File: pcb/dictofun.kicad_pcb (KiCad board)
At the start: 4 copper layers, 40 x 20 mm, 132 parts, among them J1 Conn_01x01_Female, J3 USB_B_Micro, J4 Conn_01x02_Socket, J5 Conn_01x03_Socket, Q1 PMOS, U2 W25Q128JWPIQ, U3 TPS63802DLAR, U4 BQ24078RGTR, U5 RV-4162-C7, U6 SN74LVC1G79DBVT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

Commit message: Design Freeze DF 1.4
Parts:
- S1: footprint _other:SW_KMR221GLFS -> df_components:SW_KMR221GLFS
- U3: footprint _other:VREG_TPS63802DLAR -> df_components:VREG_TPS63802DLAR
- moved RN3 0.12 mm to (125.0, 96.5)
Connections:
- U5 pad 2: /RTC_CLKOUT -> unconnected-(U5-CLKOUT-Pad2)
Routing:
- net Net-(D4-BK): track 3.55 -> 4.55 mm
- net /Power/FF_Q: track 4.91 -> 5.69 mm
- net /PDM_CLK: track 12.6 -> 13.3 mm
- net Net-(D4-GK): track 3.81 -> 4.35 mm

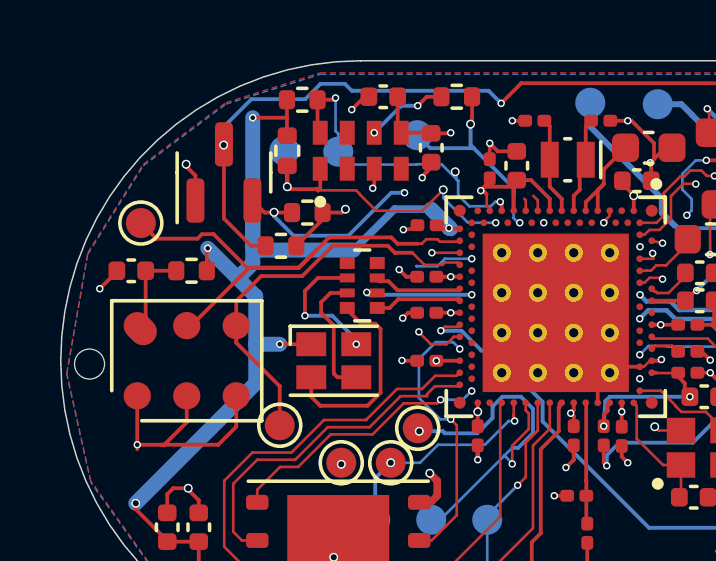
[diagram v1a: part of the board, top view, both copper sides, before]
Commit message: fixed error: RTC PFET could shorten battery to the ground
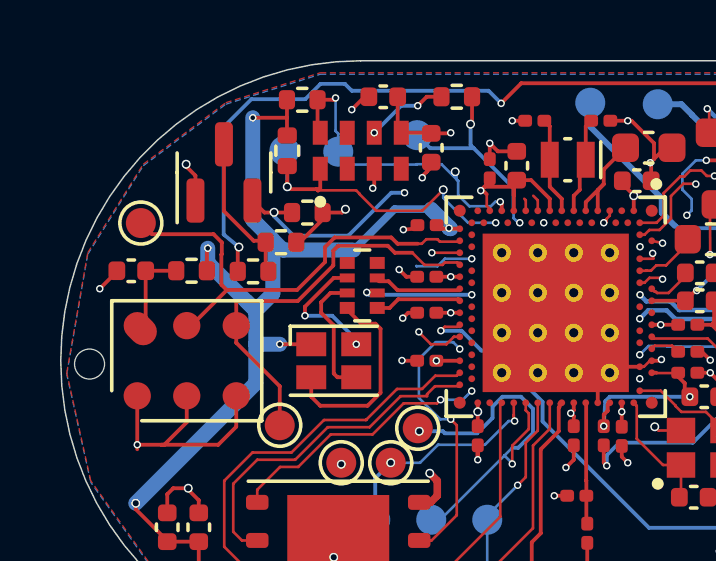
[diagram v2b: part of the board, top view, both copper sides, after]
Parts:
- added R25: 330, Resistor_SMD:R_0402_1005Metric, F.Cu at (121.4, 96.0)
- moved R24 0.12 mm to (122.3, 95.0)
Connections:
- Q1 pad 3: VREG_EN -> Net-(Q1-S)
- R24 pad 2: VREG_EN -> Net-(Q1-S)
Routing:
- net Net-(Q1-S): track 0.00 -> 5.10 mm
- net /PDM_DATA: track 17.4 -> 15.4 mm
- net VCC: track 132.3 -> 133.2 mm

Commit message: fixed another issue (added current limiting resistor, added testpoint for button control)
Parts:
- added TP33: TestPoint, TestPoint:TestPoint_Pad_D1.0mm, B.Cu at (143.8, 99.0)
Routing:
- net /BUTTON_INPUT: vias 2 -> 3
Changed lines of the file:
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@@
     (pad_to_mask_clearance 0)
     (pcbplotparams
-      (layerselection 0x00010fc_ffffffff)
+      (layerselection 0x0001000_fffffff8)
       (plot_on_all_layers_selection 0x0000000_00000000)
       (disableapertmacros false)
@@
       (sketchpadsonfab false)
       (subtractmaskfromsilk false)
-      (outputformat 1)
+      (outputformat 3)
       (mirror false)
       (drillshape 0)
       (scaleselection 1)
-      (outputdirectory "out/v1.4/gerber")
+      (outputdirectory "out/v1.4_fixture/")
     )
   )
@@
     (descr "LED SMD 0603 (1608 Metric), square (rectangular) end terminal, IPC_7351 nominal, (Body size source: http://www.tortai-tech.com/upload/download/2011102023233369053.pdf), generated with kicad-footprint-generator")
     (tags "LED")
-    (property "LCSC" "C72043")
+    (property "LCSC" "C131282")
+    (property "Populate" "")
     (property "Sheetfile" "power.kicad_sch")
     (property "Sheetname" "Power")
@@
     (descr "Capacitor SMD 0201 (0603 Metric), square (rectangular) end terminal, IPC_7351 nominal, (Body size source: https://www.vishay.com/docs/20052/crcw0201e3.pdf), generated with kicad-footprint-generator")
     (tags "capacitor")
-    (property "LCSC" "")
+    (property "LCSC" "C161369")
     (property "Populate" "")
     (property "Sheetfile" "dictofun.kicad_sch")
@@
     (descr "Capacitor SMD 0201 (0603 Metric), square (rectangular) end terminal, IPC_7351 nominal, (Body size source: https://www.vishay.com/docs/20052/crcw0201e3.pdf), generated with kicad-footprint-generator")
     (tags "capacitor")
-    (property "LCSC" "")
+    (property "LCSC" "C384700")
     (property "Populate" "")
     (property "Sheetfile" "dictofun.kicad_sch")
@@
     (descr "Inductor SMD 0201 (0603 Metric), square (rectangular) end terminal, IPC_7351 nominal, (Body size source: https://www.vishay.com/docs/20052/crcw0201e3.pdf), generated with kicad-footprint-generator")
     (tags "inductor")
-    (property "LCSC" "")
+    (property "LCSC" "C1329438")
     (property "Populate" "")
     (property "Sheetfile" "dictofun.kicad_sch")
@@
     (property "Check_prices" "https://www.snapeda.com/parts/NRF5340-QKAA-R7/Nordic+Semiconductor+ASA/view-part/?ref=eda")
     (property "Description" "\nRF System on a Chip - SoC Dual-core Bluetooth 5.2 SoC supporting Bluetooth Low Energy, Bluetooth mesh, NFC, Thread, and Zigbee\n")
+    (property "LCSC" "C3015611")
     (property "MANUFACTURER" "Nordic Semiconductor")
     (property "MAXIMUM_PACKAGE_HEIGHT" "0.85mm")
@@
   )
   (footprint "TestPoint:TestPoint_Pad_D1.0mm" (layer "B.Cu")
+    (at 143.77 99 180)
+    (descr "SMD pad as test Point, diameter 1.0mm")
+    (tags "test point SMD pad")
+    (property "Sheetfile" "dictofun.kicad_sch")
+    (property "Sheetname" "")
+    (property "ki_description" "test point")
+    (property "ki_keywords" "test point tp")
+    (attr exclude_from_pos_files)
+    (fp_text reference "TP33" (at 0 1.448) (layer "B.SilkS") hide
+        (effects (font (size 1 1) (thickness 0.15)) (justify mirror))
+    )
+    (fp_text value "TestPoint" (at 0 -1.55) (layer "B.Fab")
+        (effects (font (size 1 1) (thickness 0.15)) (justify mirror))
+    )
+    (fp_text user "${REFERENCE}" (at 0 1.45) (layer "B.Fab")
+        (effects (font (size 1 1) (thickness 0.15)) (justify mirror))
+    )
+    (fp_circle (center 0 0) (end 0 -0.7)
+      (stroke (width 0.12) (type solid)) (fill none) (layer "B.SilkS"))
+    (fp_circle (center 0 0) (end 1 0)
+      (stroke (width 0.05) (type solid)) (fill none) (layer "B.CrtYd"))
+    (pad "1" smd circle (at 0 0 180) (size 1 1) (layers "B.Cu" "B.Mask")
+      (net 49 "/BUTTON_INPUT") (pinfunction "1") (pintype "passive"))
+  )
+  (footprint "TestPoint:TestPoint_Pad_D1.0mm" (layer "B.Cu")
     (at 142 104.9 180)
     (descr "SMD pad as test Point, diameter 1.0mm")
@@
   (segment (start 122.878262 96.64) (end 120.53 96.64) (width 0.127) (layer "F.Cu") (net 48))
   (segment (start 141.55 102.22) (end 140.98 102.79) (width 0.254) (layer "F.Cu") (net 49))
+  (segment (start 143.825 98.935) (end 143.77 98.99) (width 0.254) (layer "F.Cu") (net 49))
   (segment (start 140.98 102.79) (end 140.98 103.77) (width 0.254) (layer "F.Cu") (net 49))
+  (segment (start 143.825 99.045) (end 143.825 101.05) (width 0.254) (layer "F.Cu") (net 49))
   (segment (start 153.4 99.8) (end 153.41 99.79) (width 0.127) (layer "F.Cu") (net 49))
   (segment (start 154.1 98.48) (end 154.1 99.79) (width 0.127) (layer "F.Cu") (net 49))
@@
   (segment (start 153.3 99.8) (end 153.4 99.8) (width 0.127) (layer "F.Cu") (net 49))
   (segment (start 143.825 101.275) (end 142.88 102.22) (width 0.254) (layer "F.Cu") (net 49))
-  (segment (start 143.825 96.95) (end 143.825 101.05) (width 0.254) (layer "F.Cu") (net 49))
+  (segment (start 143.77 98.99) (end 143.825 99.045) (width 0.254) (layer "F.Cu") (net 49))
+  (segment (start 143.825 96.95) (end 143.825 98.935) (width 0.254) (layer "F.Cu") (net 49))
   (segment (start 142.88 102.22) (end 141.55 102.22) (width 0.254) (layer "F.Cu") (net 49))
   (via (at 152.15 100.94) (size 0.25) (drill 0.15) (layers "F.Cu" "B.Cu") (net 49))
+  (via (at 143.77 98.99) (size 0.3) (drill 0.2) (layers "F.Cu" "B.Cu") (net 49))
   (via (at 143.84023 101.085418) (size 0.25) (drill 0.15) (layers "F.Cu" "B.Cu") (net 49))
   (segment (start 144.7685 101.6485) (end 144.75 101.63) (width 0.127) (layer "In1.Cu") (net 49))

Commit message: df 1.4.52840 ready for production
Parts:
- removed C30, C31, C32, C33, C34, C35, C45: 100n, Capacitor_SMD:C_0201_0603Metric
- removed C36: N.C, Capacitor_SMD:C_0201_0603Metric
- removed C37, C38, C39, C40, C44: 1u, Capacitor_SMD:C_0402_1005Metric
- removed C39(NP0)1: 100pF, Capacitor_SMD:C_0201_0603Metric
- removed C41: 2.2u, Capacitor_SMD:C_0603_1608Metric
- removed C42, C43: 4.7u, Capacitor_SMD:C_0603_1608Metric
- removed L4: 10uH, Inductor_SMD:L_0603_1608Metric
- removed L5, L6: 15nH, Inductor_SMD:L_0201_0603Metric
- removed R20: 4.7, Resistor_SMD:R_0201_0603Metric
- removed TP11, TP20, TP30, TP31: TestPoint, TestPoint:TestPoint_Pad_D1.0mm
- removed U7: NRF5340-QKAA-R7, _other:XCVR_NRF5340-QKAA-R7
- added C14: 1uF, Capacitor_SMD:C_0402_1005Metric, F.Cu at (138.8, 94.3)
- added C16: N.C, Capacitor_SMD:C_0402_1005Metric, F.Cu at (137.6, 98.7)
- added C22: 100nF, Capacitor_SMD:C_0402_1005Metric, F.Cu at (137.6, 99.7)
- added C48: N.C, Capacitor_SMD:C_0402_1005Metric, F.Cu at (134.2, 102.2)
- added C49: 820pF, Capacitor_SMD:C_0402_1005Metric, F.Cu at (131.9, 102.4)
- added C50: 4.7uF, Capacitor_SMD:C_0603_1608Metric, F.Cu at (126.8, 96.2)
- added C51: 4.7uF, Capacitor_SMD:C_0603_1608Metric, F.Cu at (128.2, 93.1)
- added C52: 4.7uF, Capacitor_SMD:C_0603_1608Metric, F.Cu at (127.5, 98.5)
- added C53: 100nF, Capacitor_SMD:C_0402_1005Metric, F.Cu at (128.4, 101.9)
- added C54: 100nF, Capacitor_SMD:C_0402_1005Metric, F.Cu at (130.0, 92.9)
- added C55: 1uF, Capacitor_SMD:C_0402_1005Metric, F.Cu at (136.5, 92.6)
- added C9: 10pF, Capacitor_SMD:C_0402_1005Metric, F.Cu at (136.7, 102.8)
- added L2: 10uH, Inductor_SMD:L_0402_1005Metric, F.Cu at (139.5, 92.7)
- added U1: nRF52840, Package_DFN_QFN:Nordic_AQFN-73-1EP_7x7mm_P0.5mm, F.Cu at (132.8, 97.5)
- C11, C12, C46, C47: footprint Capacitor_SMD:C_0201_0603Metric -> Capacitor_SMD:C_0402_1005Metric
- C13: value 10pF -> 100nF
- C28: value 100n -> 100p; footprint Capacitor_SMD:C_0201_0603Metric -> Capacitor_SMD:C_0402_1005Metric
- C29: value 100n -> 47nF; footprint Capacitor_SMD:C_0201_0603Metric -> Capacitor_SMD:C_0402_1005Metric
- C4, C5, C7, C8: value 100n -> 100nF; footprint Capacitor_SMD:C_0201_0603Metric -> Capacitor_SMD:C_0402_1005Metric
- C6: value 1u -> 1uF
- L3: value 10uH -> 15nH; footprint Inductor_SMD:L_0603_1608Metric -> Inductor_SMD:L_0402_1005Metric
- L7: footprint Inductor_SMD:L_0201_0603Metric -> Inductor_SMD:L_0402_1005Metric
- R14: value 100k -> 100K
- TP1, TP22, TP3: moved to F.Cu
- TP10, TP15, TP17, TP21, TP9: moved to B.Cu
- X2: footprint nRF52832_qfaa:BT-XTAL_2016_N -> df_components:BT-XTAL_2016_N
- moved TP16 27.2 mm to (118.7, 94.3)
- moved TP23 23.0 mm to (146.6, 108.1)
- moved TP21 18.8 mm to (137.6, 90.8), turned to 180 degrees
- moved TP28 18.5 mm to (131.0, 107.6)
- moved TP24 17.0 mm to (152.2, 91.9)
- moved C28 11.1 mm to (135.1, 102.2), turned to -90 degrees
- moved C13 10.9 mm to (135.5, 92.6), turned to 90 degrees
- moved TP4 10.2 mm to (142.9, 94.7)
- moved TP29 8.66 mm to (131.3, 107.6)
- moved TP13 8.26 mm to (140.0, 99.6), turned to 180 degrees
- moved TP27 8.09 mm to (152.6, 105.5)
- moved TP22 7.24 mm to (130.7, 105.6), turned to 0 degrees
- moved R23 7.11 mm to (129.3, 90.4)
- moved TP33 6.32 mm to (140.1, 104.2)
- moved L3 5.89 mm to (138.4, 92.7), turned to -90 degrees
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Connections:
- C10 pad 1: Net-(U7B-XC2) -> Net-(U1-XC1)
- C13 pad 1: Net-(U7B-XC1) -> /DEC1
- C28 pad 1: VCC -> /DEC3
- C29 pad 1: VCC -> /DEC4
- L3 pad 1: Net-(L3-Pad1) -> /DEC4
- L3 pad 2: Net-(U7A-DCC) -> /DEC4
- X2 pad 1: Net-(U7B-XC1) -> Net-(U1-XC1)
- X2 pad 3: Net-(U7B-XC2) -> Net-(U1-XC2)
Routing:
- net /DEC4: track 0.00 -> 22.2 mm, vias 0 -> 3
- net GND: track 271.2 -> 290.2 mm, vias 58 -> 55
- net V_charger: track 30.2 -> 47.1 mm
- net VCC: track 133.2 -> 118.4 mm, vias 24 -> 17
- net VREG_EN: track 62.2 -> 75.1 mm, vias 7 -> 3
- net /DBG_RX: track 30.5 -> 40.6 mm, vias 3 -> 2
- net Net-(U1-XC1): track 0.00 -> 9.64 mm
- net Net-(U7A-VBUS): track 8.08 -> 0.00 mm, vias 3 -> 0
- net /LED_RED: track 2.84 -> 10.9 mm, vias 0 -> 2
- net VBAT_LEVEL: track 21.8 -> 14.1 mm, vias 2 -> 0
- net /BUTTON_INPUT: track 21.8 -> 29.5 mm, vias 3 -> 4
- net /LED_GREEN: track 2.89 -> 10.5 mm, vias 0 -> 2
- net /N_RESET: track 7.53 -> 0.00 mm, vias 2 -> 0
- net Net-(L3-Pad1): track 7.38 -> 0.00 mm, vias 2 -> 0
- net /DECUSB: track 0.00 -> 6.89 mm
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- added copper zone on B.Cu, net GND
- removed copper zone on B.Cu, net VCC
